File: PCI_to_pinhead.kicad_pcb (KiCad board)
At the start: 2 copper layers, 5 parts, among them J1 Conn_02x25_Odd_Even, J2 Conn_02x06_Odd_Even, J3 Bus_PCI_32bit_5V, J4 Conn_02x25_Odd_Even, J5 Conn_02x06_Odd_Even

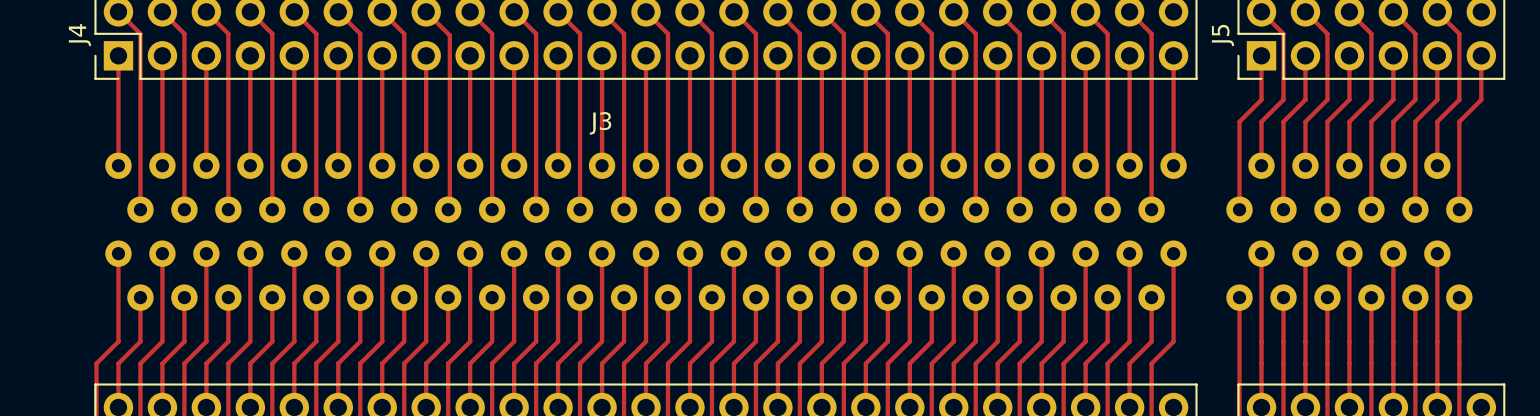
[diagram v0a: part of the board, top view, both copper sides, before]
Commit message: KiCAD 6, added holes to PCI slot and fixed pad size and hole diameters
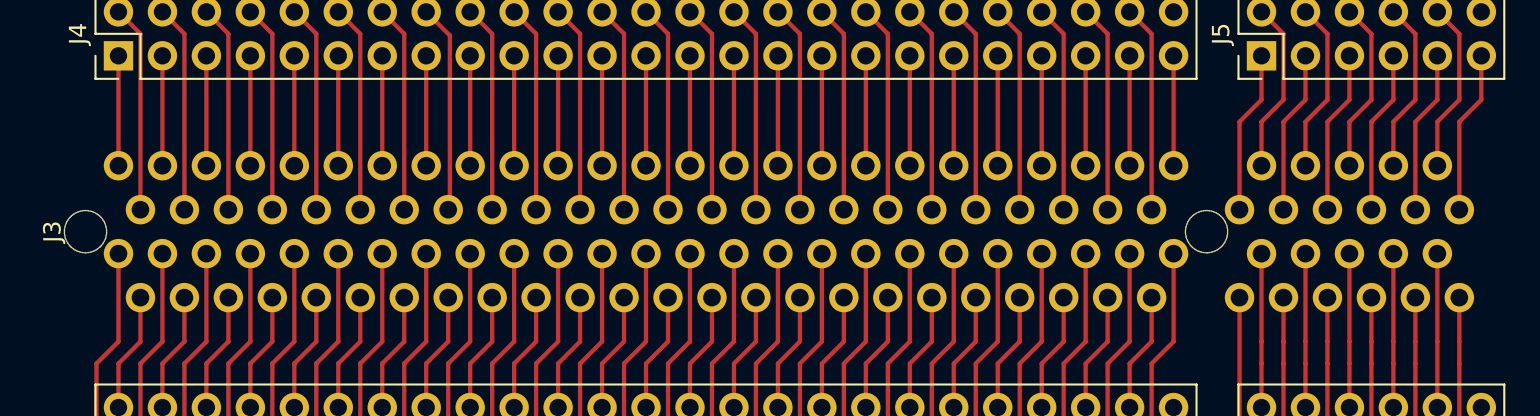
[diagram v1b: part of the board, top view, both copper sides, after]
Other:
- net class Default removed

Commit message: first attempt to order from PCBway
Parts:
- added H1: MountingHole, MountingHole:MountingHole_3.2mm_M3, F.Cu at (96.5, 99.1)
- added H2: MountingHole, MountingHole:MountingHole_3.2mm_M3, F.Cu at (175.3, 99.1)
- added H3: MountingHole, MountingHole:MountingHole_3.2mm_M3, F.Cu at (175.3, 58.4)
- added H4: MountingHole, MountingHole:MountingHole_3.2mm_M3, F.Cu at (96.5, 58.4)
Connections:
- J1 pad 50: Net-(J1-Pad50) -> unconnected-(J1-Pad50)
- J2 pad 12: Net-(J2-Pad12) -> unconnected-(J2-Pad12)
- J4 pad 50: Net-(J4-Pad50) -> unconnected-(J4-Pad50)
- J5 pad 12: Net-(J5-Pad12) -> unconnected-(J5-Pad12)
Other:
- board outline added: 90 x 50 mm
